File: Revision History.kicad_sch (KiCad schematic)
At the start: 0 parts

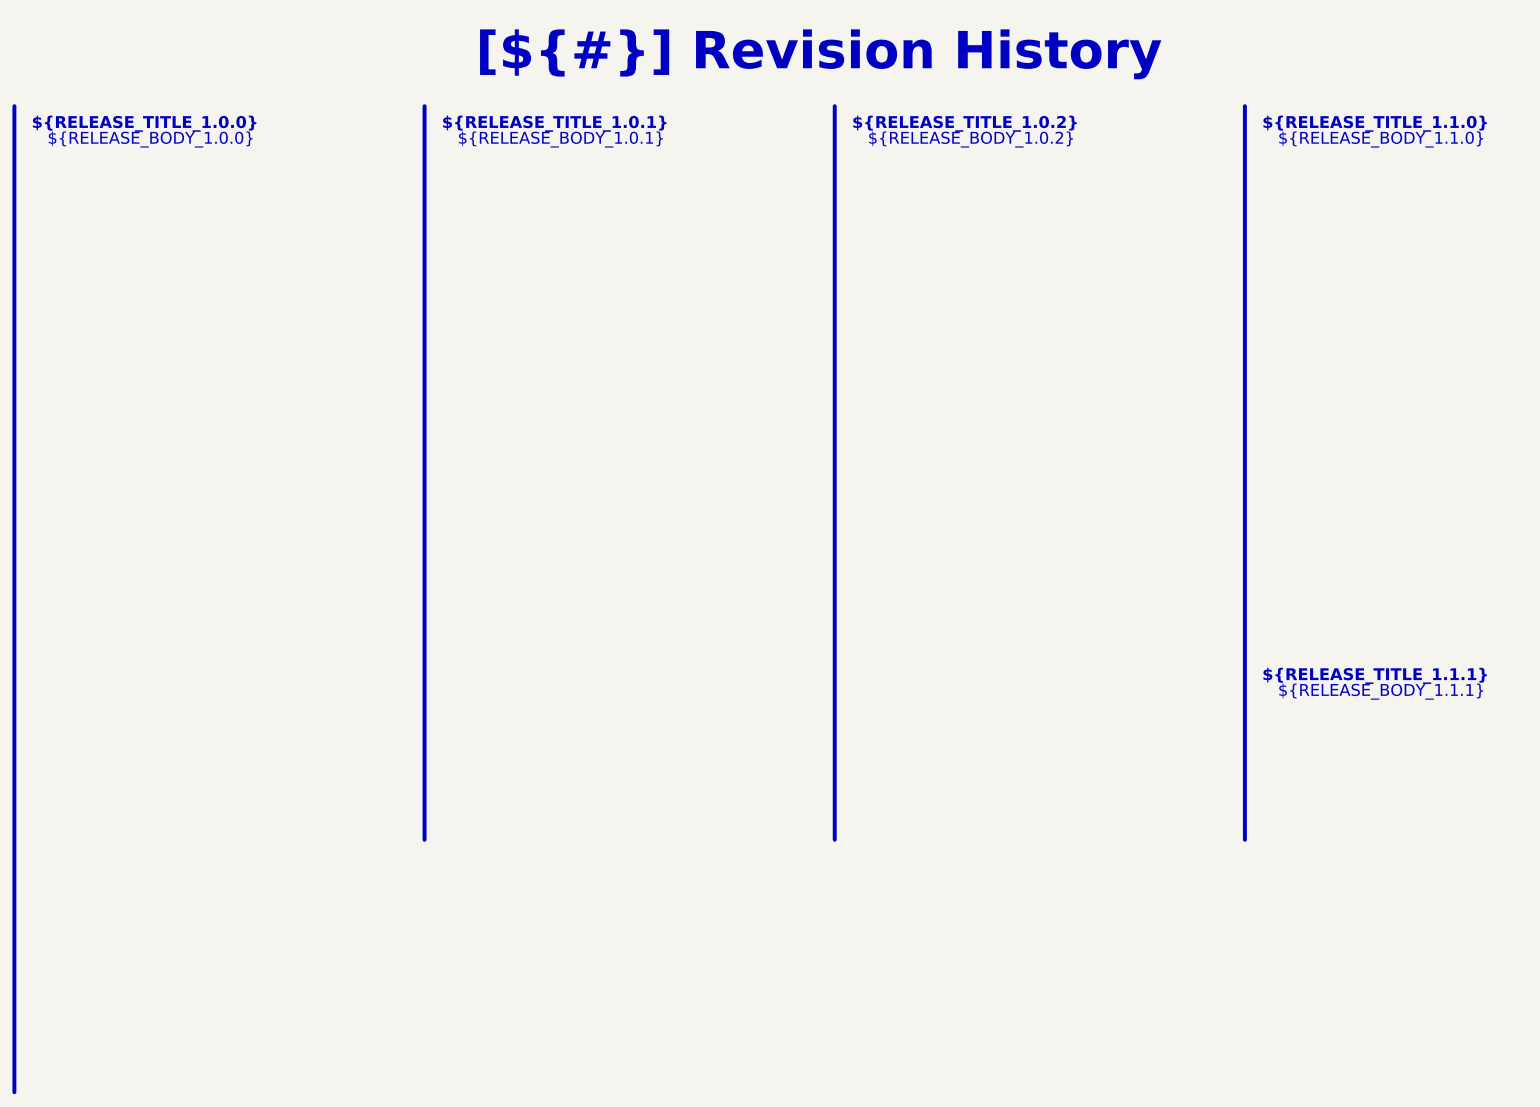
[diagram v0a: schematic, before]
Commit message: Updated files without navigate_results
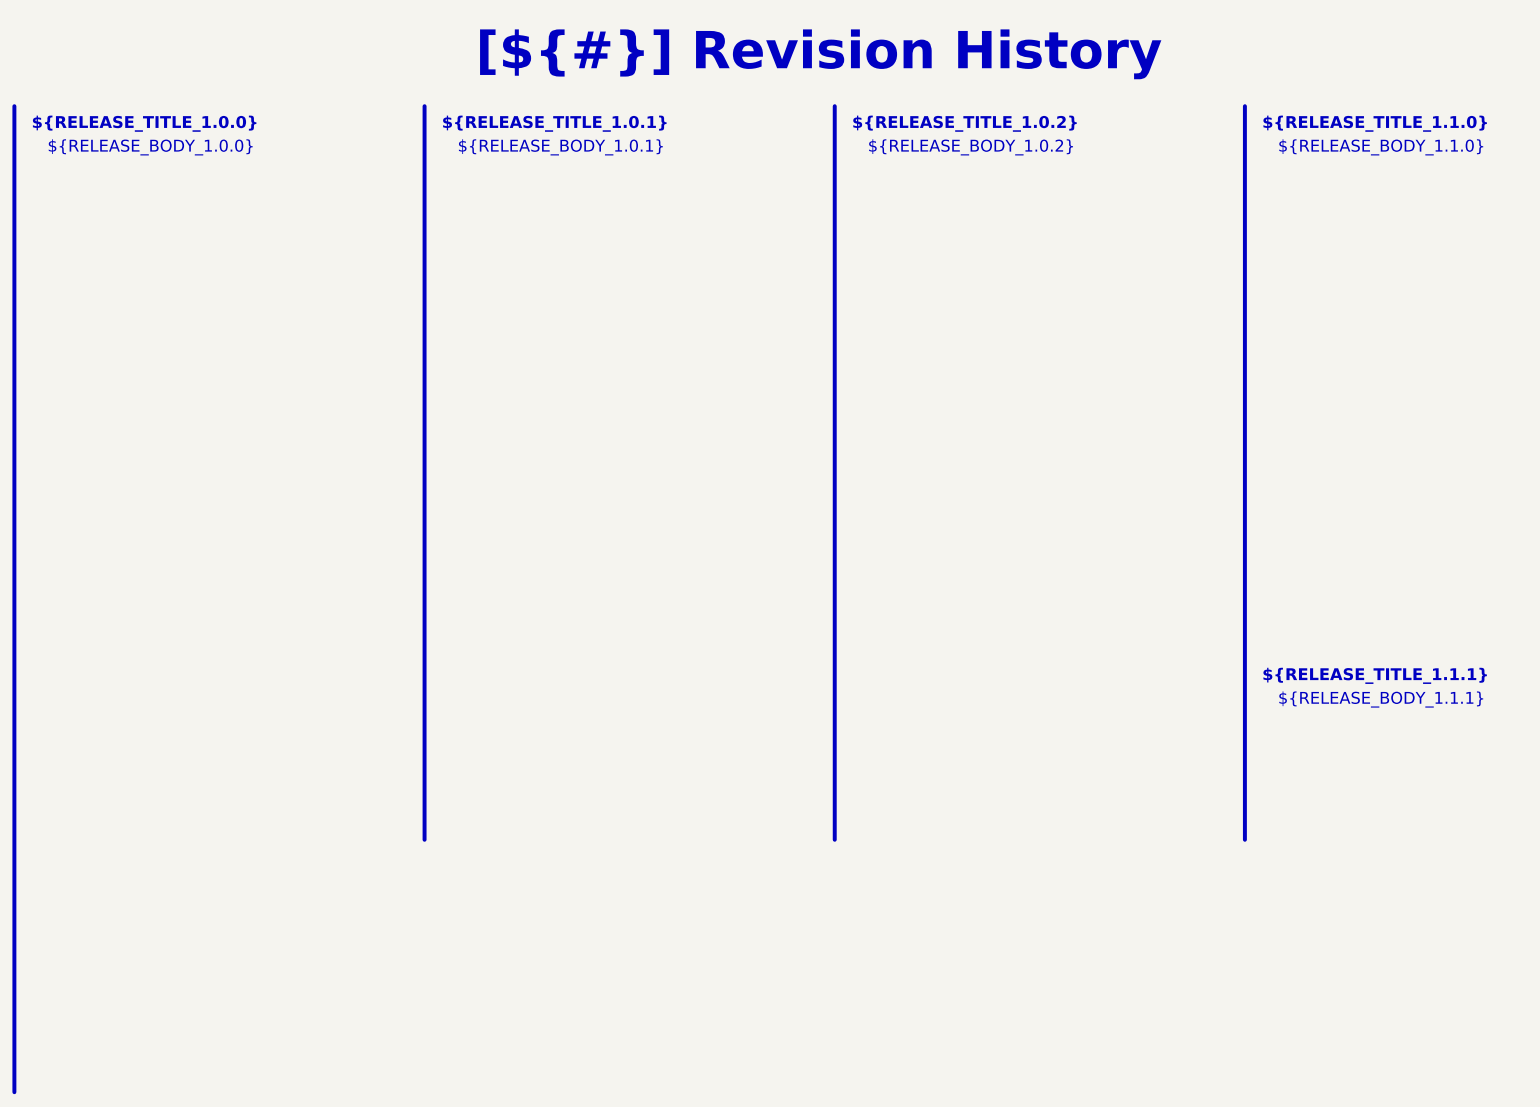
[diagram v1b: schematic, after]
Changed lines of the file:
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@@
 	(text_box "${RELEASE_BODY_1.1.0}"
 		(exclude_from_sim no)
-		(at 220.98 34.29 0)
-		(size 58.42 85.09)
+		(at 220.98 35.56 0)
+		(size 58.42 81.28)
 		(stroke
 			(width -0.0001)
@@
 	(text_box "${RELEASE_BODY_1.0.0}"
 		(exclude_from_sim no)
-		(at 22.86 34.29 0)
-		(size 58.42 149.86)
+		(at 22.86 35.56 0)
+		(size 58.42 146.05)
 		(stroke
 			(width -0.0001)
@@
 	(text_box "${RELEASE_BODY_1.1.1}"
 		(exclude_from_sim no)
-		(at 220.98 123.19 0)
-		(size 58.42 27.94)
+		(at 220.98 124.46 0)
+		(size 58.42 24.13)
 		(stroke
 			(width -0.0001)
@@
 	(text_box "${RELEASE_BODY_1.0.2}"
 		(exclude_from_sim no)
-		(at 154.94 34.29 0)
-		(size 58.42 115.57)
+		(at 154.94 35.56 0)
+		(size 58.42 111.76)
 		(stroke
 			(width -0.0001)
@@
 	(text_box "${RELEASE_BODY_1.0.1}"
 		(exclude_from_sim no)
-		(at 88.9 34.29 0)
-		(size 58.42 109.22)
+		(at 88.9 35.56 0)
+		(size 57.15 105.41)
 		(stroke
 			(width -0.0001)
